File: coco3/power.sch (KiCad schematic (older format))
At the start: 16 parts, among them CN7 Conn_01x03_Male, SW1 SW_DPDT_x2

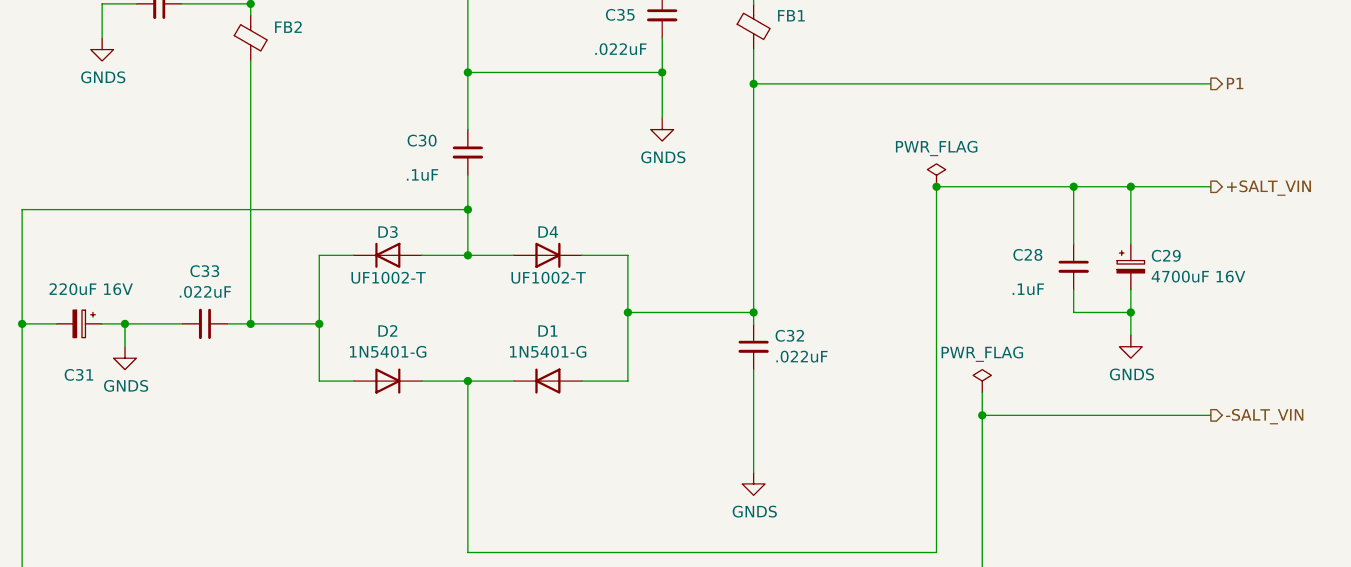
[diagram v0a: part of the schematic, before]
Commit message: -repplaced a whole bunch of THT components with SMT components
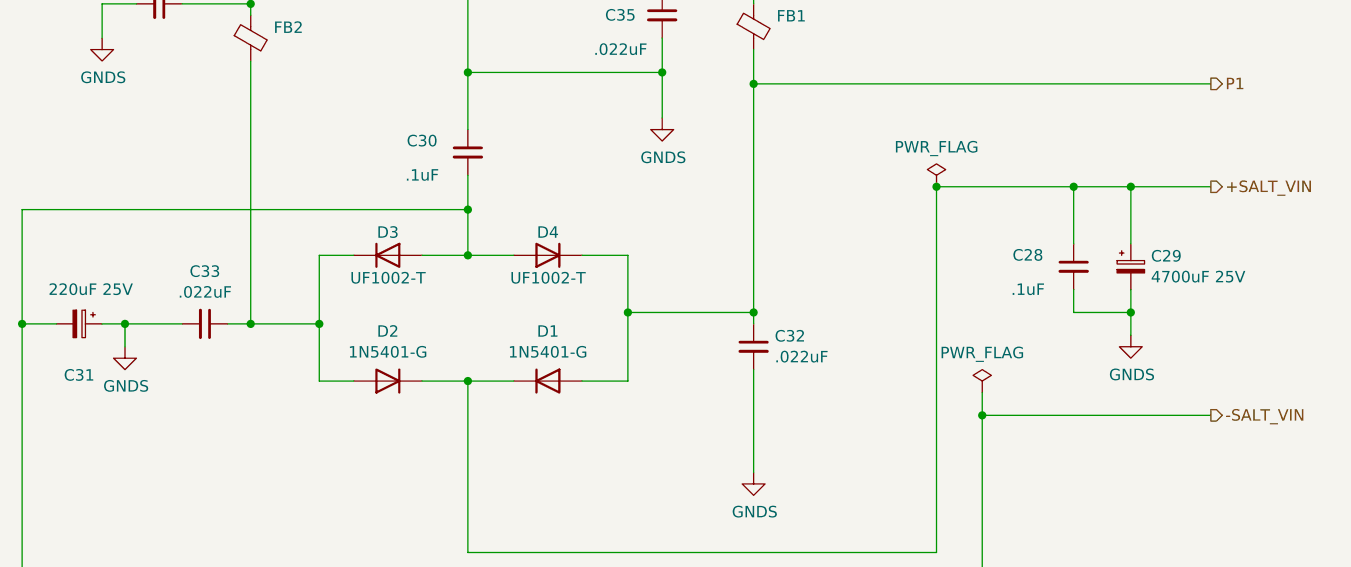
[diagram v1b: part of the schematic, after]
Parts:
- C28, C30: footprint Capacitor_THT:C_Disc_D4.7mm_W2.5mm_P5.00mm -> Capacitor_SMD:C_0805_2012Metric_Pad1.18x1.45mm_HandSolder; Manufacturer part# FG28C0G1H103JNT06 -> CL21A106KAYNNNE; Vendor digikey -> JLCPCB; Vendor part# 445-173474-1-ND -> C15850
- C29: value 4700uF 16V -> 4700uF 25V; footprint Capacitor_THT:CP_Radial_D12.5mm_P5.00mm -> Capacitor_SMD:CP_Elec_4x5.3; Manufacturer part# 16PK4700MEFC12.5X25 -> VEJ472M1ETR-1821; Vendor digikey -> JLCPCB; Vendor part# 1189-1123-ND -> C249676
- C31: value 220uF 16V -> 220uF 25V; footprint Capacitor_THT:CP_Radial_D8.0mm_P5.00mm -> Capacitor_SMD:CP_Elec_8x10; Manufacturer part# URS1C221MPD1TA -> VEJ221M1ETR-0810; Vendor digikey -> JLCPCB; Vendor part# 493-15896-1-ND -> C134765
- C32, C33, C35, C36: footprint Capacitor_THT:C_Disc_D8.0mm_W2.5mm_P5.00mm -> Capacitor_SMD:C_0805_2012Metric_Pad1.18x1.45mm_HandSolder; Manufacturer part# C317C223M5U5TA7301 -> CL21B223KBANNNC; Vendor digikey -> JLCPCB; Vendor part# 399-14073-1-ND -> C1729
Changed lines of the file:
@@
 F 0 "C35" H 5600 2800 50  0000 L CNN
 F 1 ".022uF" H 5550 2650 50  0000 L CNN
-F 2 "Capacitor_THT:C_Disc_D8.0mm_W2.5mm_P5.00mm" H 5850 2800 50  0001 C CNN
-F 3 "https://api.kemet.com/component-edge/download/datasheet/C317C223M5U5TA7301.pdf" H 5850 2800 50  0001 C CNN
-F 4 "digikey" H 5850 2800 50  0001 C CNN "Vendor"
-F 5 "399-14073-1-ND" H 5850 2800 50  0001 C CNN "Vendor part#"
-F 6 "C317C223M5U5TA7301" H 5850 2800 50  0001 C CNN "Manufacturer part#"
+F 2 "Capacitor_SMD:C_0805_2012Metric_Pad1.18x1.45mm_HandSolder" H 5850 2800 50  0001 C CNN
+F 3 "https://datasheet.lcsc.com/lcsc/1810191222_Samsung-Electro-Mechanics-CL21B223KBANNNC_C1729.pdf" H 5850 2800 50  0001 C CNN
+F 4 "JLCPCB" H 5850 2800 50  0001 C CNN "Vendor"
+F 5 "C1729" H 5850 2800 50  0001 C CNN "Vendor part#"
+F 6 "CL21B223KBANNNC" H 5850 2800 50  0001 C CNN "Manufacturer part#"
 	1    5850 2800
 	1    0    0    -1
@@
 F 0 "C36" V 3421 2750 50  0000 C CNN
 F 1 ".022uF" V 3512 2750 50  0000 C CNN
-F 2 "Capacitor_THT:C_Disc_D8.0mm_W2.5mm_P5.00mm" H 3650 2750 50  0001 C CNN
-F 3 "https://api.kemet.com/component-edge/download/datasheet/C317C223M5U5TA7301.pdf" H 3650 2750 50  0001 C CNN
-F 4 "digikey" H 3650 2750 50  0001 C CNN "Vendor"
-F 5 "399-14073-1-ND" H 3650 2750 50  0001 C CNN "Vendor part#"
-F 6 "C317C223M5U5TA7301" H 3650 2750 50  0001 C CNN "Manufacturer part#"
+F 2 "Capacitor_SMD:C_0805_2012Metric_Pad1.18x1.45mm_HandSolder" H 3650 2750 50  0001 C CNN
+F 3 "https://datasheet.lcsc.com/lcsc/1810191222_Samsung-Electro-Mechanics-CL21B223KBANNNC_C1729.pdf" H 3650 2750 50  0001 C CNN
+F 4 "JLCPCB" H 3650 2750 50  0001 C CNN "Vendor"
+F 5 "C1729" H 3650 2750 50  0001 C CNN "Vendor part#"
+F 6 "CL21B223KBANNNC" H 3650 2750 50  0001 C CNN "Manufacturer part#"
 	1    3650 2750
 	0    1    1    0
@@
 F 0 "C33" V 3621 4150 50  0000 C CNN
 F 1 ".022uF" V 3712 4150 50  0000 C CNN
-F 2 "Capacitor_THT:C_Disc_D8.0mm_W2.5mm_P5.00mm" H 3850 4150 50  0001 C CNN
-F 3 "https://api.kemet.com/component-edge/download/datasheet/C317C223M5U5TA7301.pdf" H 3850 4150 50  0001 C CNN
-F 4 "digikey" H 3850 4150 50  0001 C CNN "Vendor"
-F 5 "399-14073-1-ND" H 3850 4150 50  0001 C CNN "Vendor part#"
-F 6 "C317C223M5U5TA7301" H 3850 4150 50  0001 C CNN "Manufacturer part#"
+F 2 "Capacitor_SMD:C_0805_2012Metric_Pad1.18x1.45mm_HandSolder" H 3850 4150 50  0001 C CNN
+F 3 "https://datasheet.lcsc.com/lcsc/1810191222_Samsung-Electro-Mechanics-CL21B223KBANNNC_C1729.pdf" H 3850 4150 50  0001 C CNN
+F 4 "JLCPCB" H 3850 4150 50  0001 C CNN "Vendor"
+F 5 "C1729" H 3850 4150 50  0001 C CNN "Vendor part#"
+F 6 "CL21B223KBANNNC" H 3850 4150 50  0001 C CNN "Manufacturer part#"
 	1    3850 4150
 	0    1    1    0
@@
 F 0 "C32" H 6342 4296 50  0000 L CNN
 F 1 ".022uF" H 6342 4205 50  0000 L CNN
-F 2 "Capacitor_THT:C_Disc_D8.0mm_W2.5mm_P5.00mm" H 6250 4250 50  0001 C CNN
-F 3 "https://api.kemet.com/component-edge/download/datasheet/C317C223M5U5TA7301.pdf" H 6250 4250 50  0001 C CNN
-F 4 "digikey" H 6250 4250 50  0001 C CNN "Vendor"
-F 5 "399-14073-1-ND" H 6250 4250 50  0001 C CNN "Vendor part#"
-F 6 "C317C223M5U5TA7301" H 6250 4250 50  0001 C CNN "Manufacturer part#"
+F 2 "Capacitor_SMD:C_0805_2012Metric_Pad1.18x1.45mm_HandSolder" H 6250 4250 50  0001 C CNN
+F 3 "https://datasheet.lcsc.com/lcsc/1810191222_Samsung-Electro-Mechanics-CL21B223KBANNNC_C1729.pdf" H 6250 4250 50  0001 C CNN
+F 4 "JLCPCB" H 6250 4250 50  0001 C CNN "Vendor"
+F 5 "C1729" H 6250 4250 50  0001 C CNN "Vendor part#"
+F 6 "CL21B223KBANNNC" H 6250 4250 50  0001 C CNN "Manufacturer part#"
 	1    6250 4250
 	1    0    0    -1
@@
 F 0 "C30" H 4800 3450 50  0000 C CNN
 F 1 ".1uF" H 4800 3300 50  0000 C CNN
-F 2 "Capacitor_THT:C_Disc_D4.7mm_W2.5mm_P5.00mm" H 5000 3400 50  0001 C CNN
-F 3 " https://product.tdk.com/info/en/catalog/datasheets/leadmlcc_halogenfree_fg_en.pdf?ref_disty=digikey" H 5000 3400 50  0001 C CNN
-F 4 "digikey" V 5000 3400 50  0001 C CNN "Vendor"
-F 5 "445-173474-1-ND" V 5000 3400 50  0001 C CNN "Vendor part#"
-F 6 "FG28C0G1H103JNT06" V 5000 3400 50  0001 C CNN "Manufacturer part#"
+F 2 "Capacitor_SMD:C_0805_2012Metric_Pad1.18x1.45mm_HandSolder" H 5000 3400 50  0001 C CNN
+F 3 "https://datasheet.lcsc.com/lcsc/1811121310_Samsung-Electro-Mechanics-CL21A106KAYNNNE_C15850.pdf" H 5000 3400 50  0001 C CNN
+F 4 "JLCPCB" V 5000 3400 50  0001 C CNN "Vendor"
+F 5 "C15850" V 5000 3400 50  0001 C CNN "Vendor part#"
+F 6 "CL21A106KAYNNNE" V 5000 3400 50  0001 C CNN "Manufacturer part#"
 	1    5000 3400
 	1    0    0    -1
@@
 F 0 "C28" H 7450 3950 50  0000 C CNN
 F 1 ".1uF" H 7450 3800 50  0000 C CNN
-F 2 "Capacitor_THT:C_Disc_D4.7mm_W2.5mm_P5.00mm" H 7650 3900 50  0001 C CNN
-F 3 " https://product.tdk.com/info/en/catalog/datasheets/leadmlcc_halogenfree_fg_en.pdf?ref_disty=digikey" H 7650 3900 50  0001 C CNN
-F 4 "digikey" V 7650 3900 50  0001 C CNN "Vendor"
-F 5 "445-173474-1-ND" V 7650 3900 50  0001 C CNN "Vendor part#"
-F 6 "FG28C0G1H103JNT06" V 7650 3900 50  0001 C CNN "Manufacturer part#"
+F 2 "Capacitor_SMD:C_0805_2012Metric_Pad1.18x1.45mm_HandSolder" H 7650 3900 50  0001 C CNN
+F 3 "https://datasheet.lcsc.com/lcsc/1811121310_Samsung-Electro-Mechanics-CL21A106KAYNNNE_C15850.pdf" H 7650 3900 50  0001 C CNN
+F 4 "JLCPCB" V 7650 3900 50  0001 C CNN "Vendor"
+F 5 "C15850" V 7650 3900 50  0001 C CNN "Vendor part#"
+F 6 "CL21A106KAYNNNE" V 7650 3900 50  0001 C CNN "Manufacturer part#"
 	1    7650 3900
 	1    0    0    -1
@@
 P 3300 4150
 F 0 "C31" V 3525 4150 50  0000 C CNN
-F 1 "220uF  16V" V 3150 4200 50  0000 C CNN
-F 2 "Capacitor_THT:CP_Radial_D8.0mm_P5.00mm" H 3300 4150 50  0001 C CNN
-F 3 "http://nichicon-us.com/english/products/pdfs/e-urs.pdf" H 3300 4150 50  0001 C CNN
-F 4 "digikey" H 3300 4150 50  0001 C CNN "Vendor"
-F 5 "493-15896-1-ND" H 3300 4150 50  0001 C CNN "Vendor part#"
-F 6 "URS1C221MPD1TA" H 3300 4150 50  0001 C CNN "Manufacturer part#"
+F 1 "220uF  25V" V 3150 4200 50  0000 C CNN
+F 2 "Capacitor_SMD:CP_Elec_8x10" H 3300 4150 50  0001 C CNN
+F 3 " https://datasheet.lcsc.com/lcsc/1809291333_Lelon-VEJ221M1ETR-0810_C134765.pdf" H 3300 4150 50  0001 C CNN
+F 4 "JLCPCB" H 3300 4150 50  0001 C CNN "Vendor"
+F 5 "C134765" H 3300 4150 50  0001 C CNN "Vendor part#"
+F 6 "VEJ221M1ETR-0810" H 3300 4150 50  0001 C CNN "Manufacturer part#"
 	1    3300 4150
 	0    1    1    0
@@
 AR Path="/603CF7B8/60F7D30F" Ref="C?"  Part="1"
 F 0 "C29" H 7988 3946 50  0000 L CNN
-F 1 "4700uF 16V" H 7988 3855 50  0000 L CNN
-F 2 "Capacitor_THT:CP_Radial_D12.5mm_P5.00mm" H 7900 3900 50  0001 C CNN
-F 3 "http://www.rubycon.co.jp/en/catalog/e_pdfs/aluminum/e_pk.pdf" H 7900 3900 50  0001 C CNN
-F 4 "digikey" H 7900 3900 50  0001 C CNN "Vendor"
-F 5 "1189-1123-ND" H 7900 3900 50  0001 C CNN "Vendor part#"
-F 6 "16PK4700MEFC12.5X25" H 7900 3900 50  0001 C CNN "Manufacturer part#"
+F 1 "4700uF 25V" H 7988 3855 50  0000 L CNN
+F 2 "Capacitor_SMD:CP_Elec_4x5.3" H 7900 3900 50  0001 C CNN
+F 3 "https://datasheet.lcsc.com/lcsc/1811051717_Lelon-VEJ472M1ETR-1821_C249676.pdf" H 7900 3900 50  0001 C CNN
+F 4 "JLCPCB" H 7900 3900 50  0001 C CNN "Vendor"
+F 5 "C249676" H 7900 3900 50  0001 C CNN "Vendor part#"
+F 6 "VEJ472M1ETR-1821" H 7900 3900 50  0001 C CNN "Manufacturer part#"
 	1    7900 3900
 	1    0    0    -1

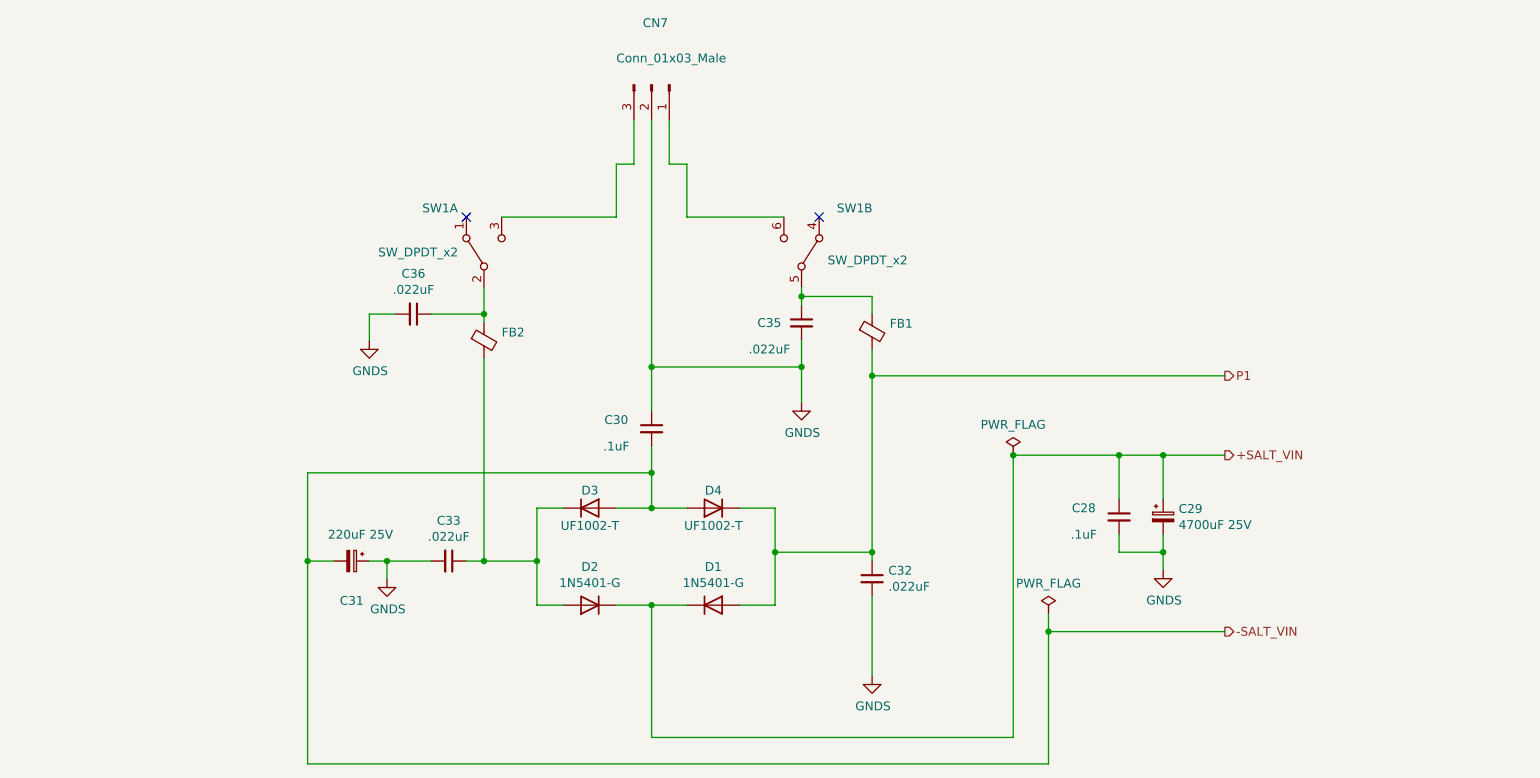
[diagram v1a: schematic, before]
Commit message: -converted more components from THT to SMD -replaced SALT chip with replacement circuitry
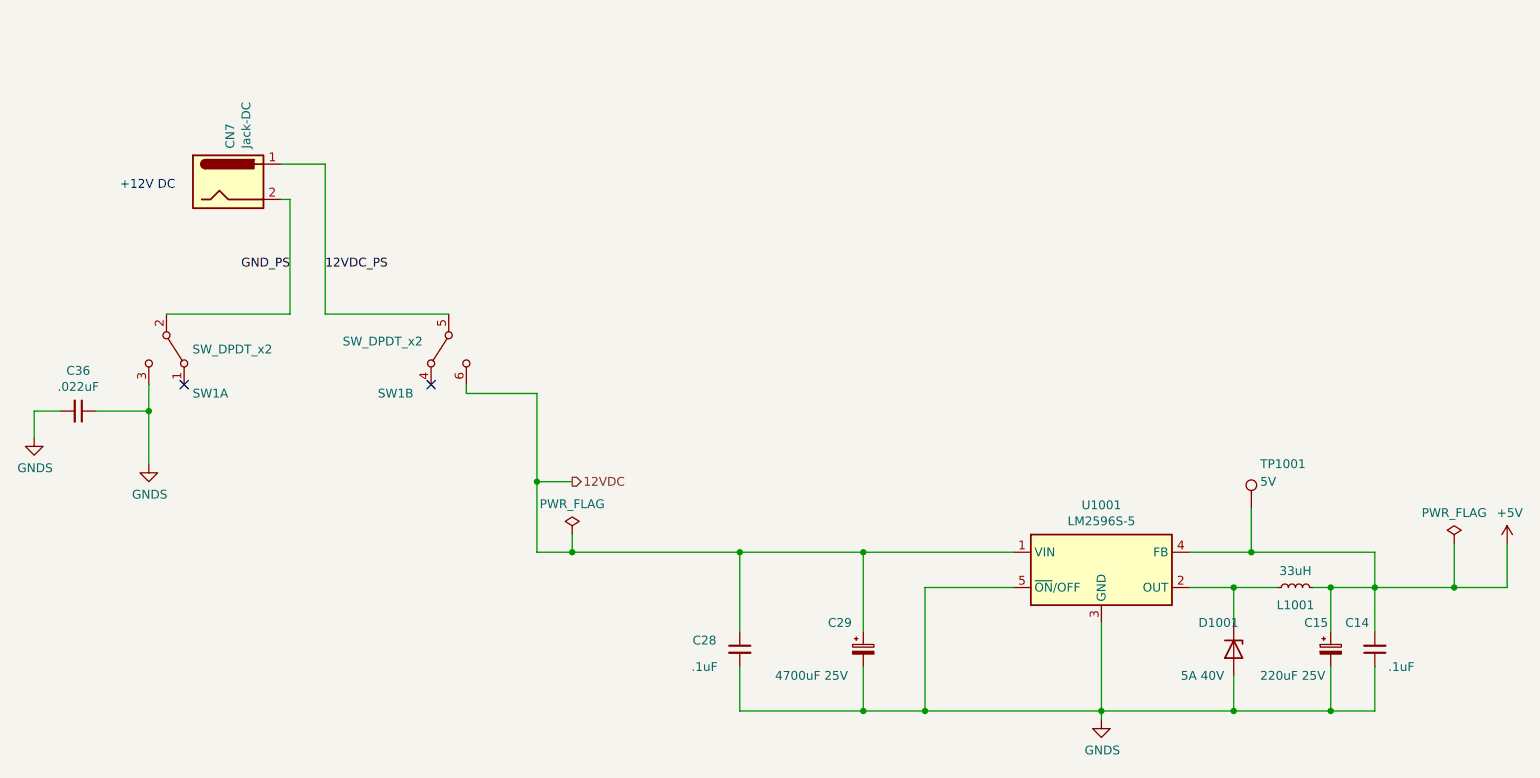
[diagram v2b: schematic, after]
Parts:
- removed C30: .1uF, Capacitor_SMD:C_0805_2012Metric_Pad1.18x1.45mm_HandSolder, symbol Device:C_Small
- removed C31: 220uF 25V, Capacitor_SMD:CP_Elec_8x10, symbol Device:CP_Small
- removed C32, C33, C35: .022uF, Capacitor_SMD:C_0805_2012Metric_Pad1.18x1.45mm_HandSolder, symbol Device:C_Small
- removed CN7: Conn_01x03_Male, Connector_Molex:Molex_KK-396_A-41791-0003_1x03_P3.96mm_Vertical, symbol Connector:Conn_01x03_Male
- removed D1, D2: 1N5401-G, Diode_THT:D_DO-201AD_P15.24mm_Horizontal, symbol Diode:1N5401
- removed D3, D4: UF1002-T, Diode_THT:D_DO-41_SOD81_P10.16mm_Horizontal, symbol Diode:1N4002
- removed FB1, FB2: (no value), coco2:FB_28L0138-10R-10, symbol Device:Ferrite_Bead_Small
- added C14: .1uF, Capacitor_SMD:C_0805_2012Metric_Pad1.18x1.45mm_HandSolder, symbol Device:C_Small
- added C15: 220uF 25V, Capacitor_SMD:CP_Elec_8x10, symbol Device:CP_Small
- added CN7: Jack-DC, Connector_BarrelJack:BarrelJack_CUI_PJ-063AH_Horizontal, symbol Connector:Jack-DC
- added D1001: 5A 40V, Diode_SMD:D_SMB, symbol Device:D_Zener
- added L1001: 33uH, Inductor_SMD:L_Sumida_CDMC6D28_7.25x6.5mm, symbol Device:L_Small
- added TP1001: 5V, TestPoint:TestPoint_Pad_3.0x3.0mm, symbol Connector:TestPoint
- added U1001: LM2596S-5, Package_TO_SOT_SMD:TO-263-5_TabPin3, symbol Regulator_Switching:LM2596S-5
- C29: footprint Capacitor_SMD:CP_Elec_4x5.3 -> Capacitor_SMD:CP_Elec_18x22
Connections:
- net +SALT_VIN is gone; now on net 12VDC: C28.1, C29.1
- net GNDS: now also C36.1, SW1.3 (C), C14.1, C15.2, D1001.2 (A), U1001.3 (GND), U1001.5 (~ON~/OFF)
- net 12VDC_PS: now reaches SW1.5 (B)
- net 12VDC_PS: now also CN7.1
- net GND_PS: now reaches SW1.2 (B)
- net GND_PS: now also CN7.2; no longer C36.1
- net 12VDC: now reaches SW1.6 (C)
- net 12VDC: now also U1001.1 (VIN)
- new net: D1001.1 (K), L1001.1, U1001.2 (OUT)
- new net +5V: C14.2, C15.1, L1001.2, TP1001.1, U1001.4 (FB)
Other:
- note added: "+12V DC"
- moved on the sheet: C28, C29, C36, SW1A, SW1B

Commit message: routed the board
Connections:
- net GND_PS is gone; now on net GNDS: CN7.2, SW1.2 (B)
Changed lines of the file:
@@
 Wire Wire Line
 	4350 3200 4350 3700
+$Comp
+L power:GNDS #PWR?
+U 1 1 613B4395
+P 2950 3100
+F 0 "#PWR?" H 2950 2850 50  0001 C CNN
+F 1 "GNDS" H 2955 2927 50  0000 C CNN
+F 2 "" H 2950 3100 50  0001 C CNN
+F 3 "" H 2950 3100 50  0001 C CNN
+	1    2950 3100
+	1    0    0    -1
+$EndComp
+Wire Wire Line
+	2950 2750 2950 3100
+Connection ~ 2950 2750
 $EndSCHEMATC
